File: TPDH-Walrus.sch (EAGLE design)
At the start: 44 parts, among them Q2 DMG3404, U1 MS5803-14BA, U2 SN65HVD33RHL, U4 MCP3421A3, U5 TPS79733, U6 MAX6070AAUT18, U7 TXS0102DQM

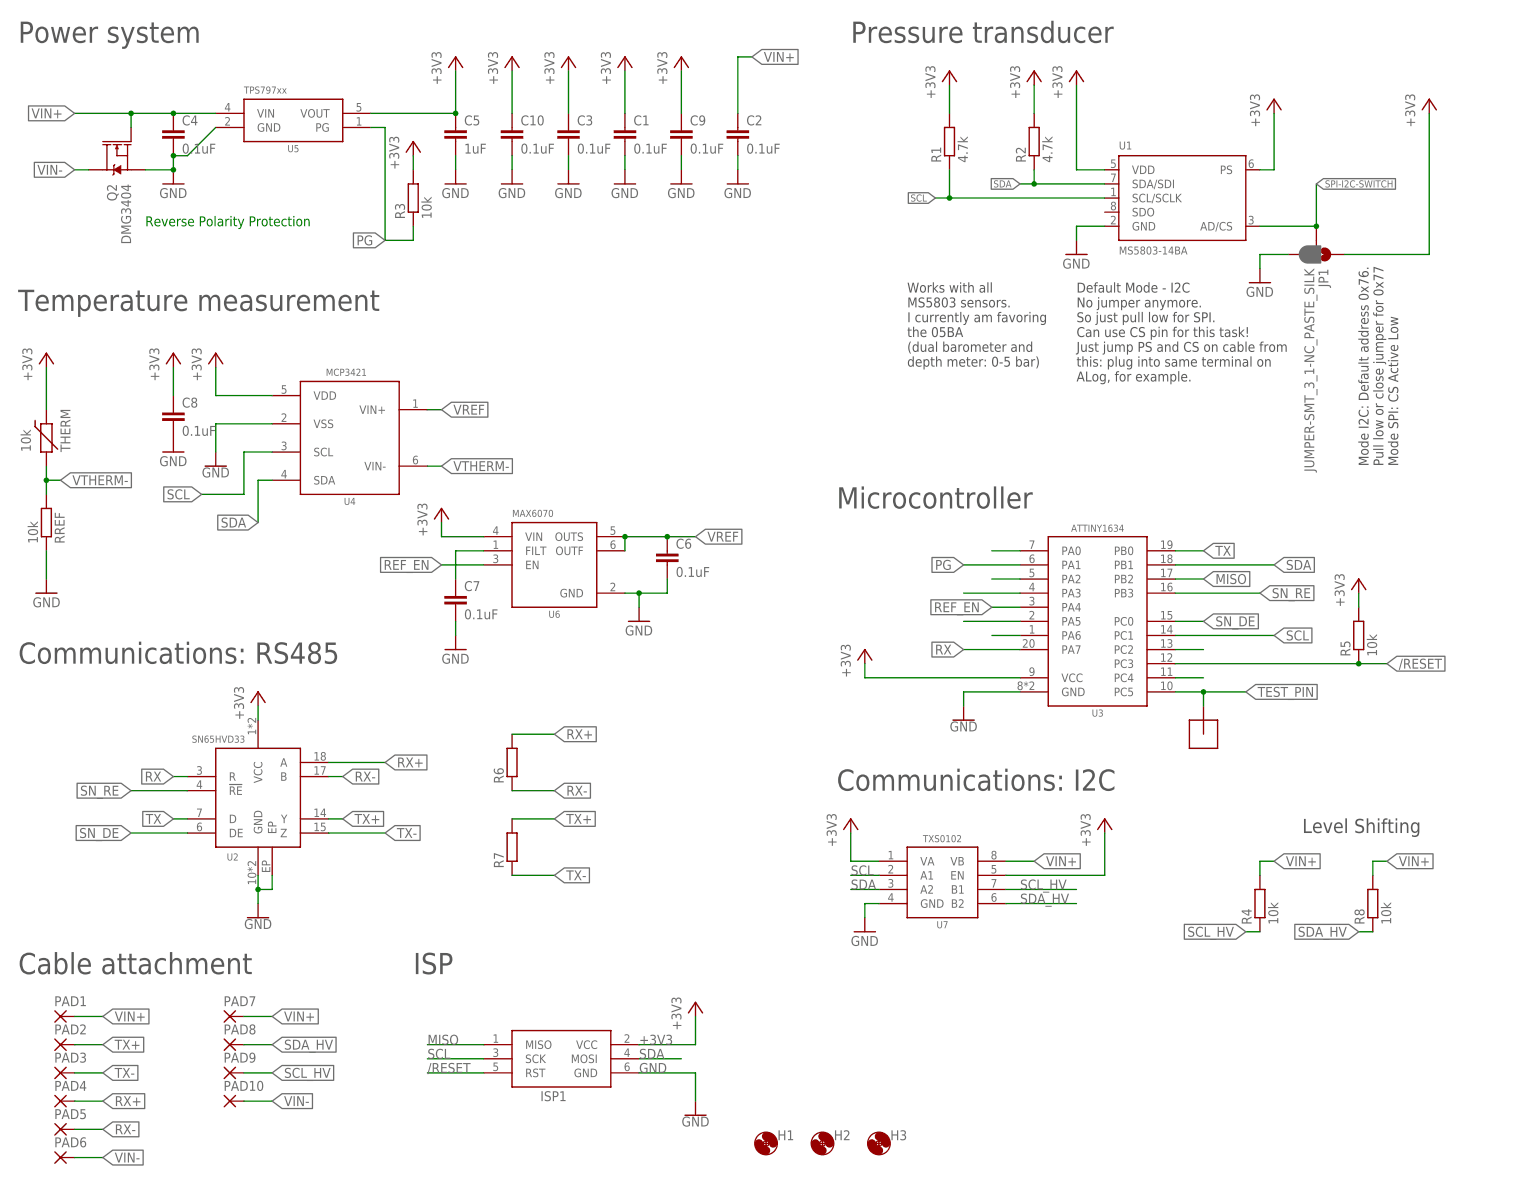
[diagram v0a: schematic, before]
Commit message: Major revision Add 10 uF cap Reroute to keep decoupling caps near ICs Change schematic to reflect the above reorganization Reroute to move thermistor to upper right
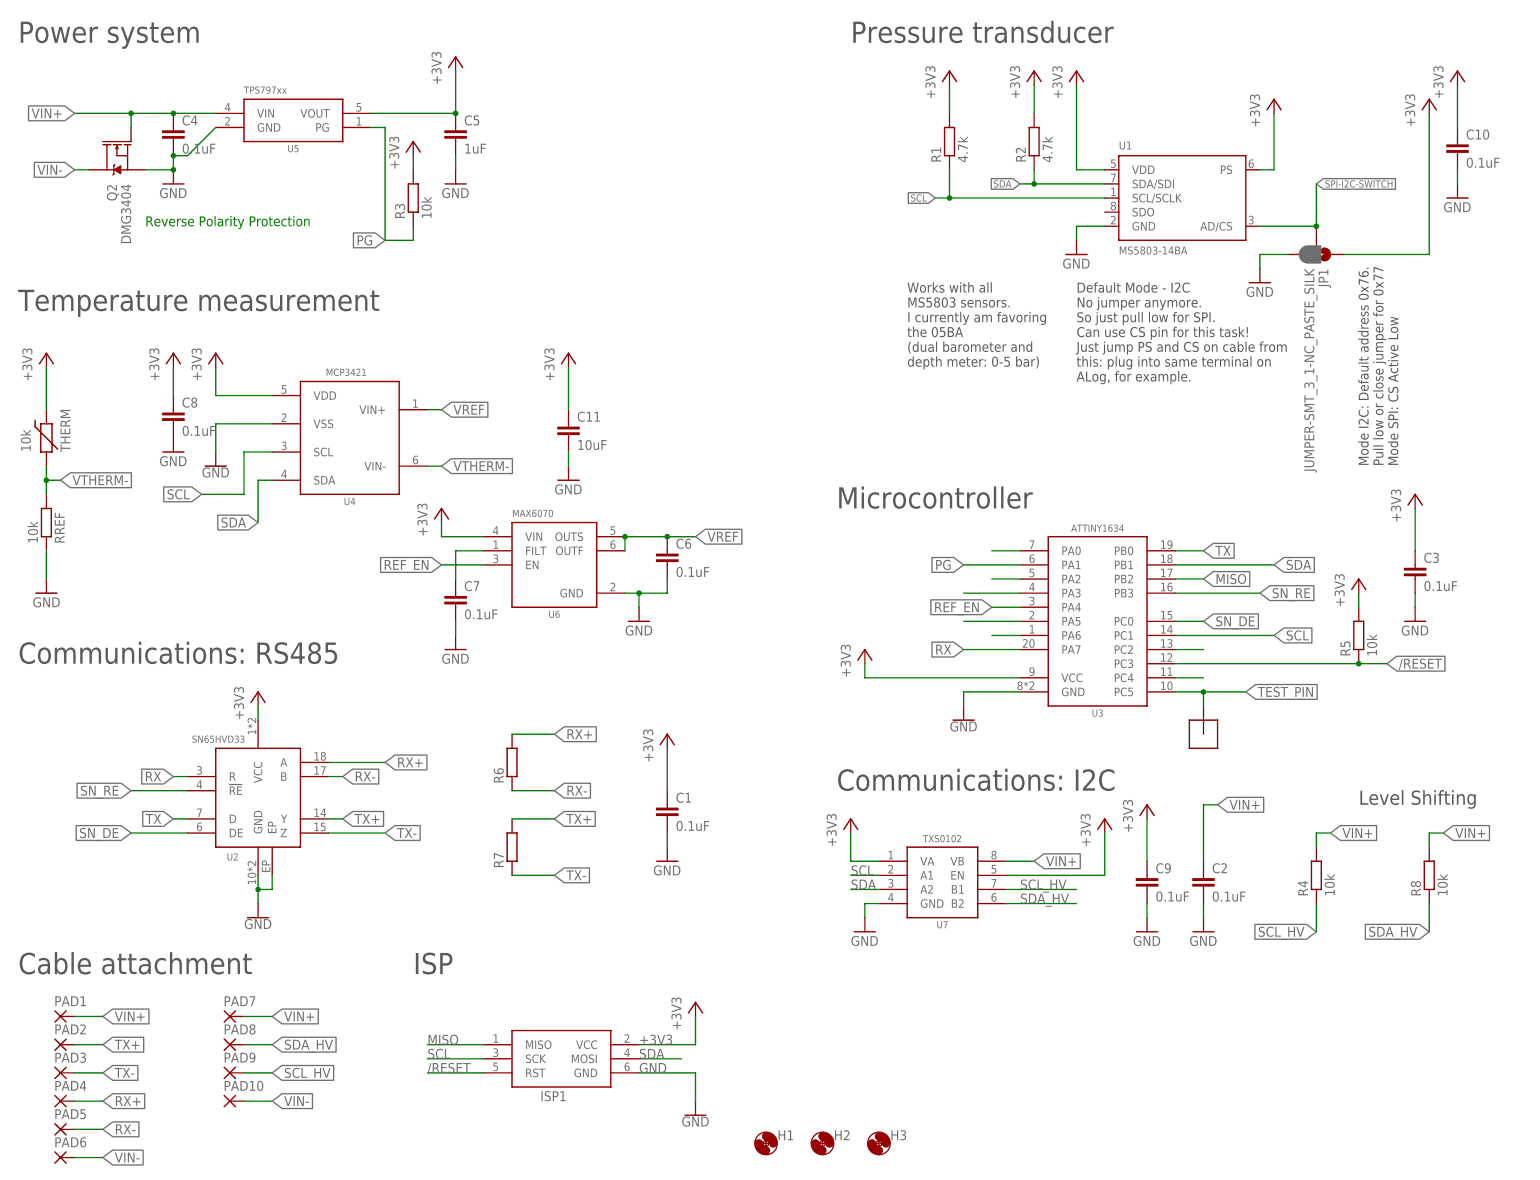
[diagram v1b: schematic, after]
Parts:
- added C11: 10uF, bschulz:C-EU10UFC0805
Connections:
- net +3V3: now also C11.1
- net GND: now also C11.2
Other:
- moved on the sheet: C1, C10, C2, C3, C9, R4, R8

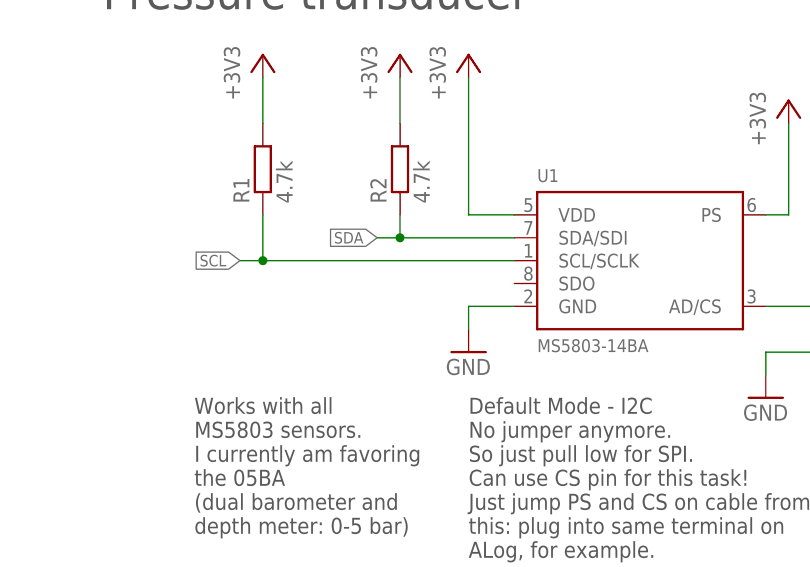
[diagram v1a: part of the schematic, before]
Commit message: add SDO for I2C
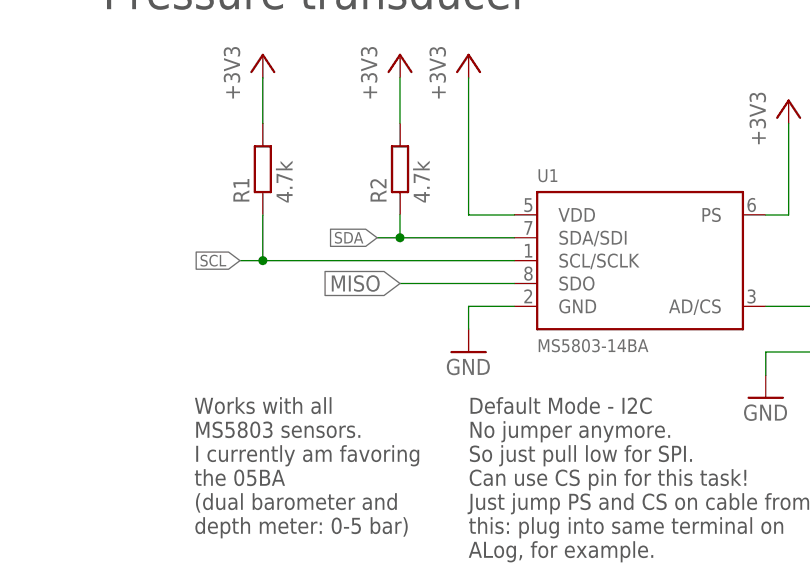
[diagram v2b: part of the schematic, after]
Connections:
- net MISO: now also U1.SDO
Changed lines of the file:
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@@
 <label x="220.98" y="109.22" size="1.778" layer="95" xref="yes"/>
+</segment>
+<segment>
+<pinref part="U1" gate="G$1" pin="SDO"/>
+<wire x1="203.2" y1="175.26" x2="190.5" y2="175.26" width="0.1524" layer="91"/>
+<label x="190.5" y="175.26" size="1.778" layer="95" rot="R180" xref="yes"/>
 </segment>
 </net>

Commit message: Routed, DRC passed
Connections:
- removed net N$15: U3.PA6
- new net N$1: U3.PA1
- net PG: now also U3.PA6; no longer U3.PA1
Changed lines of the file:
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@@
 <pinref part="U1" gate="G$1" pin="SDO"/>
 <wire x1="203.2" y1="175.26" x2="190.5" y2="175.26" width="0.1524" layer="91"/>
-<label x="190.5" y="175.26" size="1.778" layer="95" rot="R180" xref="yes"/>
+<label x="190.5" y="175.26" size="1.27" layer="95" rot="R180" xref="yes"/>
 </segment>
 </net>
@@
 </segment>
 <segment>
-<pinref part="U3" gate="G$1" pin="PA1"/>
-<wire x1="187.96" y1="111.76" x2="177.8" y2="111.76" width="0.1524" layer="91"/>
-<label x="177.8" y="111.76" size="1.778" layer="95" rot="R180" xref="yes"/>
+<pinref part="U3" gate="G$1" pin="PA6"/>
+<wire x1="187.96" y1="99.06" x2="167.64" y2="99.06" width="0.1524" layer="91"/>
+<label x="167.64" y="99.06" size="1.778" layer="95" rot="R180" xref="yes"/>
 </segment>
 </net>
@@
 <pinref part="U3" gate="G$1" pin="PA5"/>
 <wire x1="187.96" y1="101.6" x2="177.8" y2="101.6" width="0.1524" layer="91"/>
-</segment>
-</net>
-<net name="N$15" class="0">
-<segment>
-<pinref part="U3" gate="G$1" pin="PA6"/>
-<wire x1="187.96" y1="99.06" x2="182.88" y2="99.06" width="0.1524" layer="91"/>
 </segment>
 </net>
@@
 </segment>
 </net>
+<net name="N$1" class="0">
+<segment>
+<pinref part="U3" gate="G$1" pin="PA1"/>
+<wire x1="187.96" y1="111.76" x2="177.8" y2="111.76" width="0.1524" layer="91"/>
+</segment>
+</net>

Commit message: Partial ERC
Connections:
- removed net N$1: U3.PA1
- removed net N$10: U3.PC4
- removed net N$14: U3.PA5
- removed net N$2: U3.PA0
- removed net N$7: U3.PA2
- removed net N$8: U3.PC2
- removed net N$9: U3.PA3
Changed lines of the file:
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@@
-</segment>
-</net>
-<net name="N$8" class="0">
-<segment>
-<pinref part="U3" gate="G$1" pin="PC2"/>
-<wire x1="215.9" y1="96.52" x2="220.98" y2="96.52" width="0.1524" layer="91"/>
-</segment>
-</net>
-<net name="N$10" class="0">
-<segment>
-<pinref part="U3" gate="G$1" pin="PC4"/>
-<wire x1="215.9" y1="91.44" x2="220.98" y2="91.44" width="0.1524" layer="91"/>
-</segment>
-</net>
-<net name="N$2" class="0">
-<segment>
-<pinref part="U3" gate="G$1" pin="PA0"/>
-<wire x1="187.96" y1="114.3" x2="182.88" y2="114.3" width="0.1524" layer="91"/>
-</segment>
-</net>
-<net name="N$7" class="0">
-<segment>
-<pinref part="U3" gate="G$1" pin="PA2"/>
-<wire x1="187.96" y1="109.22" x2="182.88" y2="109.22" width="0.1524" layer="91"/>
-</segment>
-</net>
-<net name="N$9" class="0">
-<segment>
-<pinref part="U3" gate="G$1" pin="PA3"/>
-<wire x1="187.96" y1="106.68" x2="177.8" y2="106.68" width="0.1524" layer="91"/>
-</segment>
-</net>
-<net name="N$14" class="0">
-<segment>
-<pinref part="U3" gate="G$1" pin="PA5"/>
-<wire x1="187.96" y1="101.6" x2="177.8" y2="101.6" width="0.1524" layer="91"/>
 </segment>
 </net>
@@
 </segment>
 </net>
-<net name="N$1" class="0">
-<segment>
-<pinref part="U3" gate="G$1" pin="PA1"/>
-<wire x1="187.96" y1="111.76" x2="177.8" y2="111.76" width="0.1524" layer="91"/>
-</segment>
-</net>
